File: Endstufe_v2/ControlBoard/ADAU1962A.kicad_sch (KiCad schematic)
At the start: 36 parts, among them J14 DAC all outputs, J9 DNP, U13 ADAU1962AWBSTZ, Y3 24.576Mhz

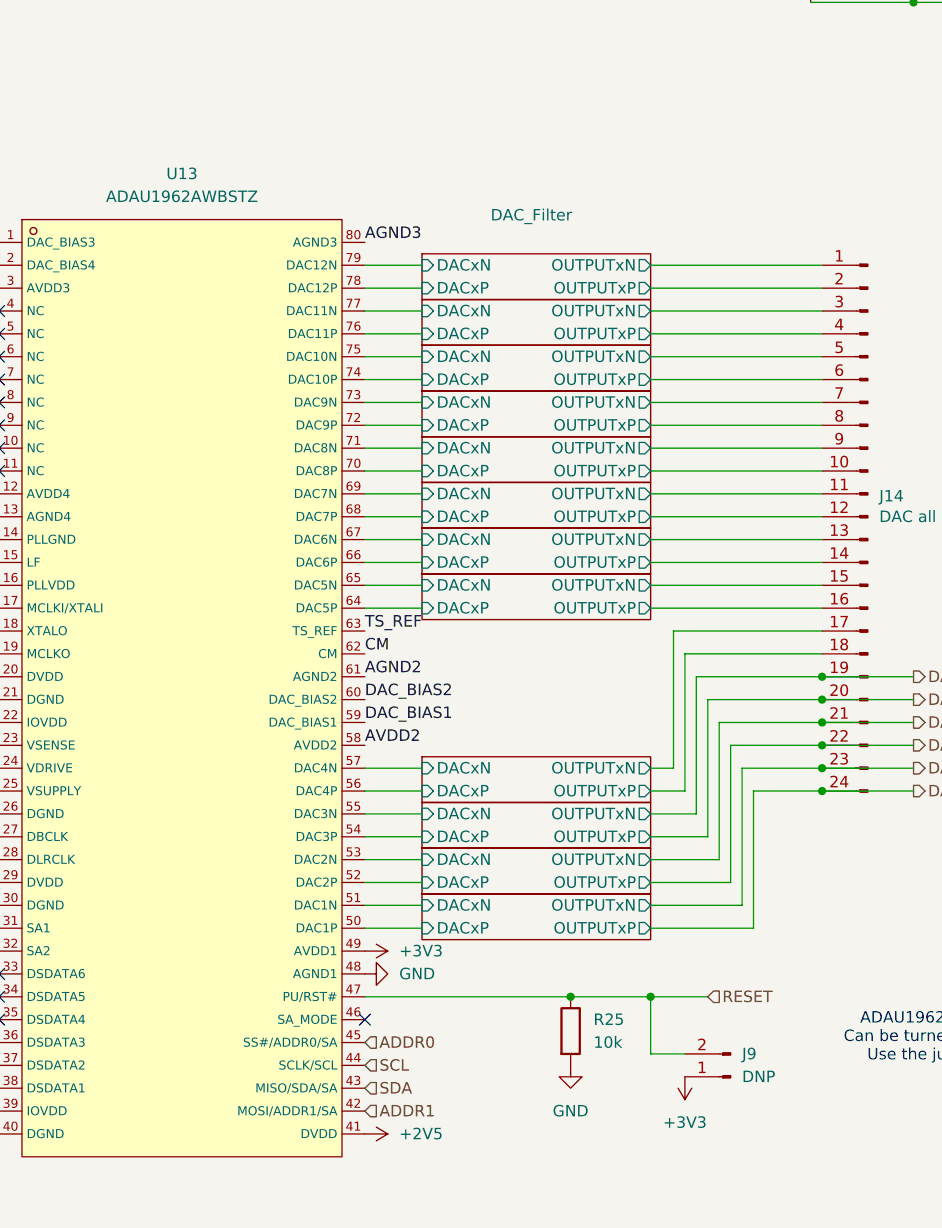
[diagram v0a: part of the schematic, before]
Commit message: Add footprints to all components
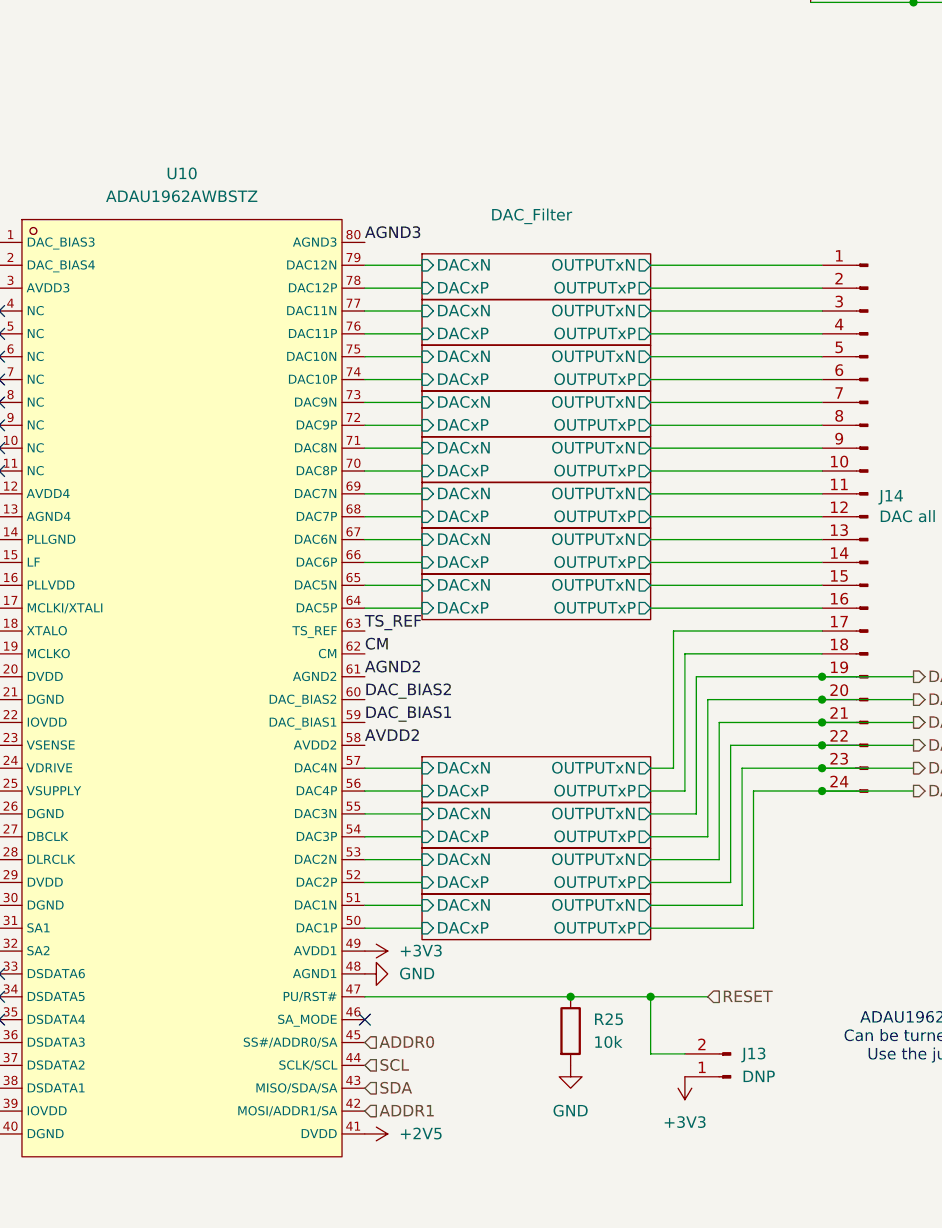
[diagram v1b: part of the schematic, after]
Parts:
- C40: footprint (none) -> Endstufe:C_0603_1608Metric
- J13: renamed from J9; footprint (none) -> Connector_PinSocket_2.54mm:PinSocket_1x02_P2.54mm_Vertical
- R22: footprint (none) -> Endstufe:R_0603_1608Metric
- TP10, TP11, TP12, TP13, TP9: footprint (none) -> TestPoint:TestPoint_Pad_D1.0mm
- renumbered U13 to U10
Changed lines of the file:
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@@
 			)
 		)
-		(property "Footprint" ""
+		(property "Footprint" "TestPoint:TestPoint_Pad_D1.0mm"
 			(at 105.41 129.54 0)
 			(effects
@@
 			)
 		)
-		(property "Footprint" ""
+		(property "Footprint" "TestPoint:TestPoint_Pad_D1.0mm"
 			(at 39.37 177.8 0)
 			(effects
@@
 			)
 		)
-		(property "Footprint" ""
+		(property "Footprint" "TestPoint:TestPoint_Pad_D1.0mm"
 			(at 105.41 132.08 0)
 			(effects
@@
 			)
 		)
-		(property "Footprint" ""
+		(property "Footprint" "TestPoint:TestPoint_Pad_D1.0mm"
 			(at 105.41 99.06 0)
 			(effects
@@
 			)
 		)
-		(property "Footprint" ""
+		(property "Footprint" "Endstufe:R_0603_1608Metric"
 			(at 43.942 71.12 90)
 			(effects
@@
 			)
 		)
-		(property "Footprint" ""
+		(property "Footprint" "TestPoint:TestPoint_Pad_D1.0mm"
 			(at 63.5 107.95 0)
 			(effects
@@
 		(dnp no)
 		(fields_autoplaced yes)
-		(property "Reference" "U13"
+		(property "Reference" "U10"
 			(at 125.73 50.8 0)
 			(effects
@@
 			(project ""
 				(path "/4f887f51-77c1-41d4-a3eb-45d362caffe1/5cb7c68c-1844-445a-b3a5-8ff13a4c7875"
-					(reference "U13")
+					(reference "U10")
 					(unit 1)
 				)
@@
 			)
 		)
-		(property "Footprint" ""
+		(property "Footprint" "Endstufe:C_0603_1608Metric"
 			(at 32.7152 78.74 0)
 			(effects
@@
 		(dnp no)
 		(fields_autoplaced yes)
-		(property "Reference" "J9"
+		(property "Reference" "J13"
 			(at 187.96 148.5899 0)
 			(effects
@@
 			)
 		)
-		(property "Footprint" ""
+		(property "Footprint" "Connector_PinSocket_2.54mm:PinSocket_1x02_P2.54mm_Vertical"
 			(at 186.69 151.13 0)
 			(effects
@@
 			(project ""
 				(path "/4f887f51-77c1-41d4-a3eb-45d362caffe1/5cb7c68c-1844-445a-b3a5-8ff13a4c7875"
-					(reference "J9")
+					(reference "J13")
 					(unit 1)
 				)

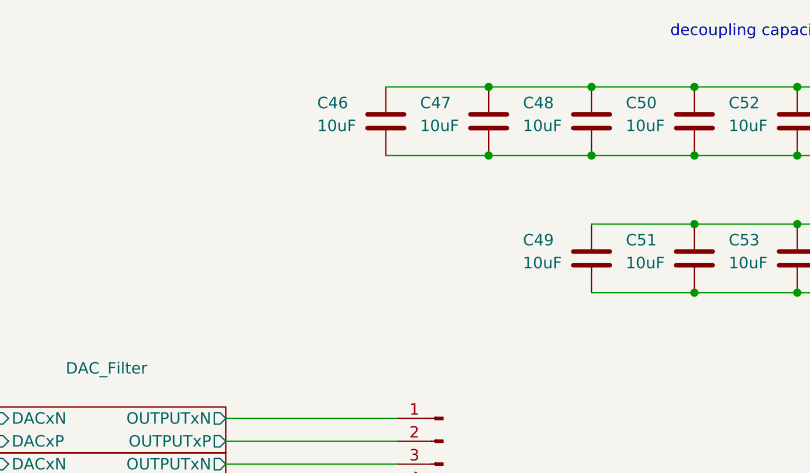
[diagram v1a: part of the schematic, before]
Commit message: Rough layout of components
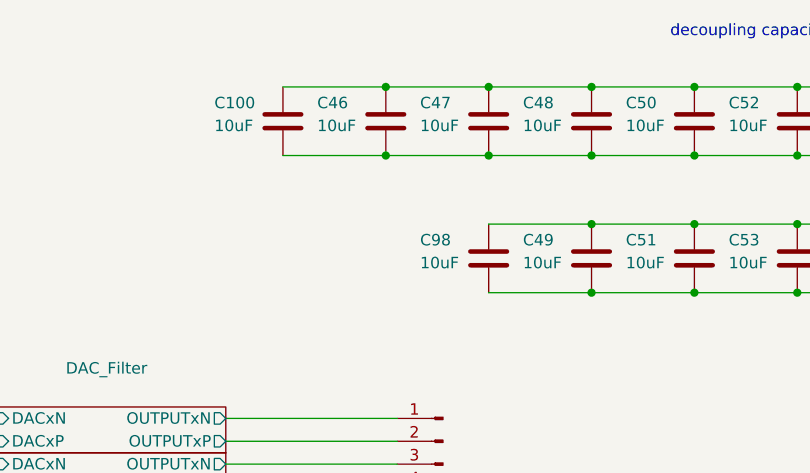
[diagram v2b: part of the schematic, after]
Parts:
- added C100, C98: 10uF, Endstufe:C_0402_1005Metric, symbol Endstufe:C
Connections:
- net +2V5: now also C98.2
- net +3V3: now also C100.2
- net GND: now also C100.1, C98.1
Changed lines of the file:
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@@
 	)
 	(junction
+		(at 195.58 24.13)
+		(diameter 0)
+		(color 0 0 0 0)
+	)
+	(junction
 		(at 265.43 39.37)
 		(diameter 0)
@@
 	)
 	(junction
+		(at 218.44 46.99)
+		(diameter 0)
+		(color 0 0 0 0)
+	)
+	(junction
 		(at 168.91 142.24)
 		(diameter 0)
@@
 	)
 	(junction
+		(at 195.58 31.75)
+		(diameter 0)
+		(color 0 0 0 0)
+	)
+	(junction
 		(at 254 39.37)
 		(diameter 0)
@@
 	)
 	(junction
+		(at 218.44 39.37)
+		(diameter 0)
+		(color 0 0 0 0)
+	)
+	(junction
 		(at 241.3 24.13)
 		(diameter 0)
@@
 	(wire
 		(pts
+			(xy 184.15 31.75) (xy 195.58 31.75)
+		)
+		(stroke
+			(width 0)
+			(type default)
+		)
+	)
+	(wire
+		(pts
 			(xy 229.87 46.99) (xy 241.3 46.99)
 		)
@@
 	(wire
 		(pts
+			(xy 184.15 24.13) (xy 195.58 24.13)
+		)
+		(stroke
+			(width 0)
+			(type default)
+		)
+	)
+	(wire
+		(pts
 			(xy 44.45 115.57) (xy 29.21 115.57)
 		)
@@
 	(wire
 		(pts
+			(xy 207.01 39.37) (xy 218.44 39.37)
+		)
+		(stroke
+			(width 0)
+			(type default)
+		)
+	)
+	(wire
+		(pts
 			(xy 177.8 66.04) (xy 196.85 66.04)
 		)
@@
 	(wire
 		(pts
+			(xy 207.01 46.99) (xy 218.44 46.99)
+		)
+		(stroke
+			(width 0)
+			(type default)
+		)
+	)
+	(wire
+		(pts
 			(xy 195.58 31.75) (xy 207.01 31.75)
 		)
@@
 	(symbol
 		(lib_id "Endstufe:C")
+		(at 184.15 27.94 0)
+		(unit 1)
+		(exclude_from_sim no)
+		(in_bom yes)
+		(on_board yes)
+		(dnp no)
+		(property "Reference" "C100"
+			(at 176.53 25.908 0)
+			(effects
+				(font
+					(size 1.27 1.27)
+				)
+				(justify left)
+			)
+		)
+		(property "Value" "10uF"
+			(at 176.53 28.448 0)
+			(effects
+				(font
+					(size 1.27 1.27)
+				)
+				(justify left)
+			)
+		)
+		(property "Footprint" "Endstufe:C_0402_1005Metric"
+			(at 185.1152 31.75 0)
+			(effects
+				(font
+					(size 1.27 1.27)
+				)
+				(hide yes)
+			)
+		)
+		(property "Datasheet" "~"
+			(at 184.15 27.94 0)
+			(effects
+				(font
+					(size 1.27 1.27)
+				)
+				(hide yes)
+			)
+		)
+		(property "Description" "Unpolarized capacitor"
+			(at 184.15 27.94 0)
+			(effects
+				(font
+					(size 1.27 1.27)
+				)
+				(hide yes)
+			)
+		)
+		(property "LCSC Part #" "C15525"
+			(at 184.15 27.94 0)
+			(effects
+				(font
+					(size 1.27 1.27)
+				)
+				(hide yes)
+			)
+		)
+		(pin "1"
+		)
+		(pin "2"
+		)
+		(instances
+			(project "ControlBoard"
+				(path "/4f887f51-77c1-41d4-a3eb-45d362caffe1/5cb7c68c-1844-445a-b3a5-8ff13a4c7875"
+					(reference "C100")
+					(unit 1)
+				)
+			)
+		)
+	)
+	(symbol
+		(lib_id "Endstufe:C")
 		(at 265.43 43.18 0)
 		(unit 1)
@@
 					(unit 1)
 				)
+			)
+		)
+	)
+	(symbol
+		(lib_id "Endstufe:C")
+		(at 207.01 43.18 0)
+		(unit 1)
+		(exclude_from_sim no)
+		(in_bom yes)
+		(on_board yes)
+		(dnp no)
+		(property "Reference" "C98"
+			(at 199.39 41.148 0)
+			(effects
+				(font
+					(size 1.27 1.27)
+				)
+				(justify left)
+			)
+		)
+		(property "Value" "10uF"
+			(at 199.39 43.688 0)
+			(effects
+				(font
+					(size 1.27 1.27)
+				)
+				(justify left)
+			)
+		)
+		(property "Footprint" "Endstufe:C_0402_1005Metric"
+			(at 207.9752 46.99 0)
+			(effects
+				(font
+					(size 1.27 1.27)
+				)
+				(hide yes)
+			)
+		)
+		(property "Datasheet" "~"
+			(at 207.01 43.18 0)
+			(effects
+				(font
+					(size 1.27 1.27)
+				)
+				(hide yes)
+			)
+		)
+		(property "Description" "Unpolarized capacitor"
+			(at 207.01 43.18 0)
+			(effects
+				(font
+					(size 1.27 1.27)
+				)
+				(hide yes)
+			)
+		)
+		(property "LCSC Part #" "C15525"
+			(at 207.01 43.18 0)
+			(effects
+				(font
+					(size 1.27 1.27)
+				)
+				(hide yes)
+			)
+		)
+		(pin "1"
+		)
+		(pin "2"
+		)
+		(instances
+			(project "ControlBoard"
+				(path "/4f887f51-77c1-41d4-a3eb-45d362caffe1/5cb7c68c-1844-445a-b3a5-8ff13a4c7875"
+					(reference "C98")
+					(unit 1)
+				)

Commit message: Change unavailable parts to available ones, optimise silkscreen, do via stiching
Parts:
- C41, C42, C45, C57, C58: footprint Capacitor_SMD:C_0402_1005Metric -> Endstufe:C_0402_1005Metric
- C43, C44: LCSC Part # C458861 -> C526980
- J13: footprint Connector_PinSocket_2.54mm:PinSocket_1x02_P2.54mm_Vertical -> Endstufe:PinSocket_1x02_P2.54mm_Vertical
- TP10, TP11, TP12, TP13, TP9: footprint TestPoint:TestPoint_Pad_D1.0mm -> Endstufe:TestPoint_Pad_D1.0mm
- U10: JLCPCB Rotation Offset (none) -> 90
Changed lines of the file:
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@@
 			)
 		)
-		(property "Footprint" "Capacitor_SMD:C_0402_1005Metric"
+		(property "Footprint" "Endstufe:C_0402_1005Metric"
 			(at 36.83 34.29 0)
 			(effects
@@
 			)
 		)
-		(property "Footprint" "TestPoint:TestPoint_Pad_D1.0mm"
+		(property "Footprint" "Endstufe:TestPoint_Pad_D1.0mm"
 			(at 105.41 129.54 0)
 			(effects
@@
 			)
 		)
-		(property "Footprint" "Capacitor_SMD:C_0402_1005Metric"
+		(property "Footprint" "Endstufe:C_0402_1005Metric"
 			(at 257.81 92.71 0)
 			(effects
@@
 			)
 		)
-		(property "Footprint" "TestPoint:TestPoint_Pad_D1.0mm"
+		(property "Footprint" "Endstufe:TestPoint_Pad_D1.0mm"
 			(at 39.37 177.8 0)
 			(effects
@@
 			)
 		)
-		(property "Footprint" "TestPoint:TestPoint_Pad_D1.0mm"
+		(property "Footprint" "Endstufe:TestPoint_Pad_D1.0mm"
 			(at 105.41 132.08 0)
 			(effects
@@
 			)
 		)
-		(property "LCSC Part #" "C458861"
+		(property "LCSC Part #" "C526980"
 			(at 44.45 119.38 0)
 			(effects
@@
 			)
 		)
-		(property "Footprint" "TestPoint:TestPoint_Pad_D1.0mm"
+		(property "Footprint" "Endstufe:TestPoint_Pad_D1.0mm"
 			(at 105.41 99.06 0)
 			(effects
@@
 			)
 		)
-		(property "Footprint" "Capacitor_SMD:C_0402_1005Metric"
+		(property "Footprint" "Endstufe:C_0402_1005Metric"
 			(at 257.81 85.09 0)
 			(effects
@@
 			)
 		)
-		(property "LCSC Part #" "C458861"
+		(property "LCSC Part #" "C526980"
 			(at 44.45 104.14 0)
 			(effects
@@
 			)
 		)
-		(property "Footprint" "Capacitor_SMD:C_0402_1005Metric"
+		(property "Footprint" "Endstufe:C_0402_1005Metric"
 			(at 46.6852 82.55 0)
 			(effects
@@
 			)
 		)
-		(property "Footprint" "TestPoint:TestPoint_Pad_D1.0mm"
+		(property "Footprint" "Endstufe:TestPoint_Pad_D1.0mm"
 			(at 63.5 107.95 0)
 			(effects
@@
 			)
 		)
-		(property "Footprint" "Capacitor_SMD:C_0402_1005Metric"
+		(property "Footprint" "Endstufe:C_0402_1005Metric"
 			(at 36.83 41.91 0)
 			(effects
@@
 			)
 		)
+		(property "JLCPCB Rotation Offset" "90"
+			(at 0 215.9 0)
+			(effects
+				(font
+					(size 1.27 1.27)
+				)
+				(hide yes)
+			)
+		)
 		(pin "29"
 		)
@@
 			)
 		)
-		(property "Footprint" "Connector_PinSocket_2.54mm:PinSocket_1x02_P2.54mm_Vertical"
+		(property "Footprint" "Endstufe:PinSocket_1x02_P2.54mm_Vertical"
 			(at 186.69 151.13 0)
 			(effects
